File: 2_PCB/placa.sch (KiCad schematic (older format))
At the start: 39 parts, among them J1 Screw_Terminal_01x02, J2 Conn_01x04_Male, J3 Screw_Terminal_01x02, J4 TestPoints, J5 Conn_01x02_Male, U1 STM32L051C8Tx, U2 Ai-Thinker-Ra-01, Y1 8 MHz, Y2 32.768 kHz

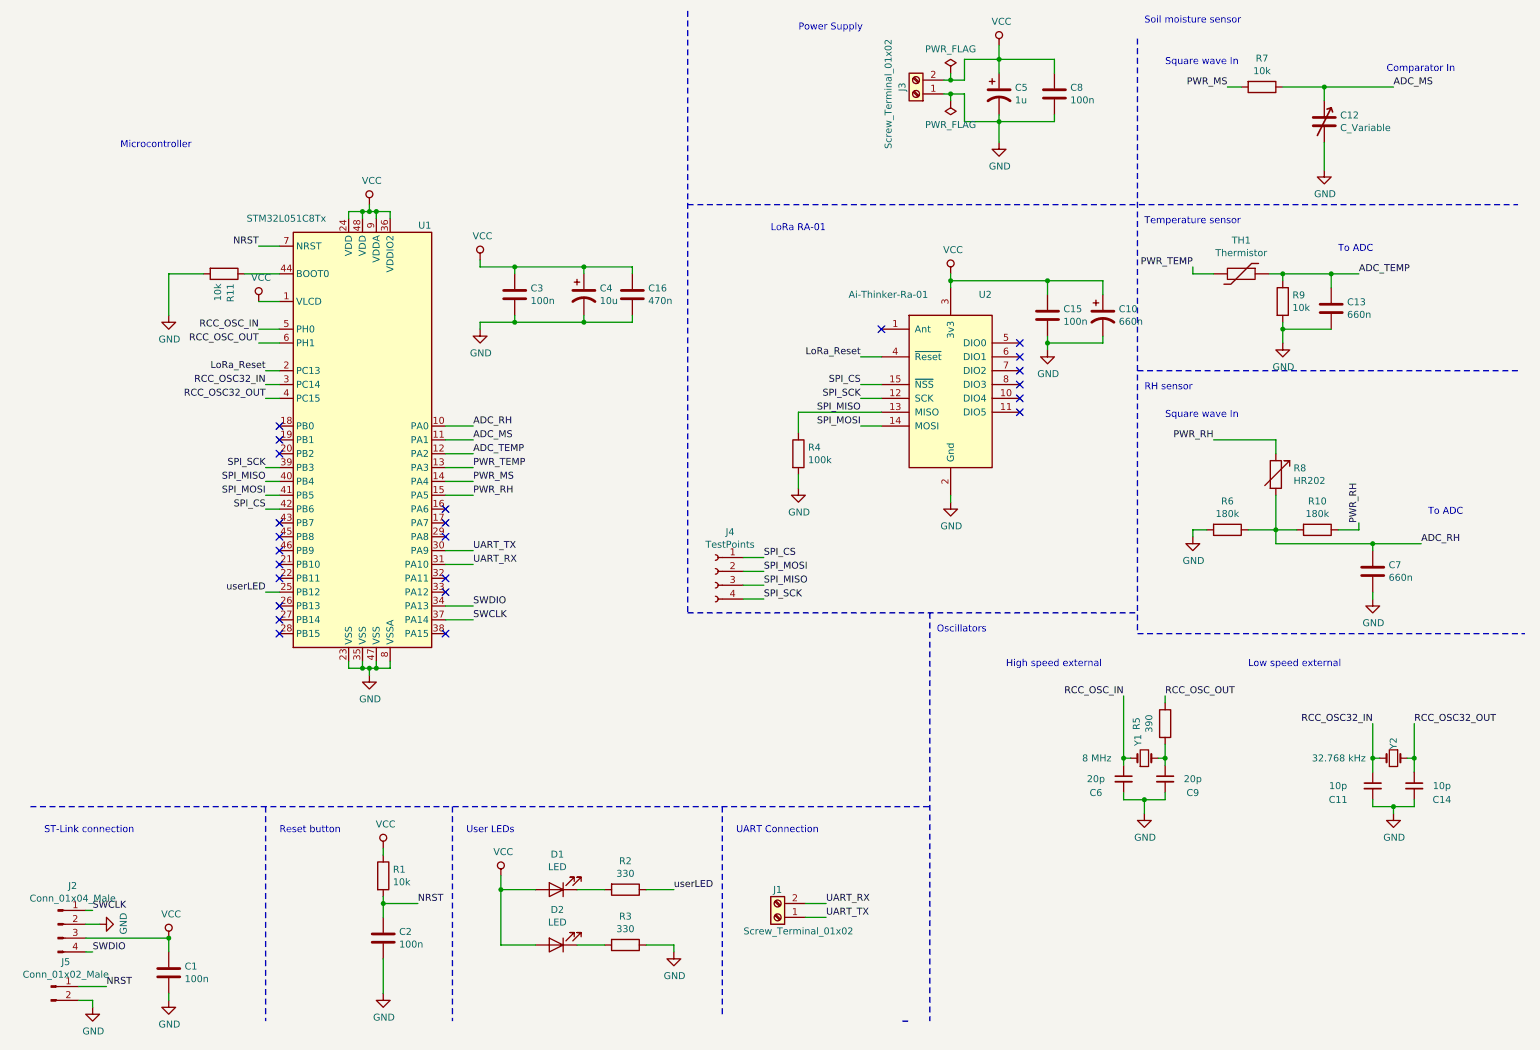
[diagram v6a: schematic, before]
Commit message: New branch for new HW revision. To add different layout, comparator for MS, change in RH circ
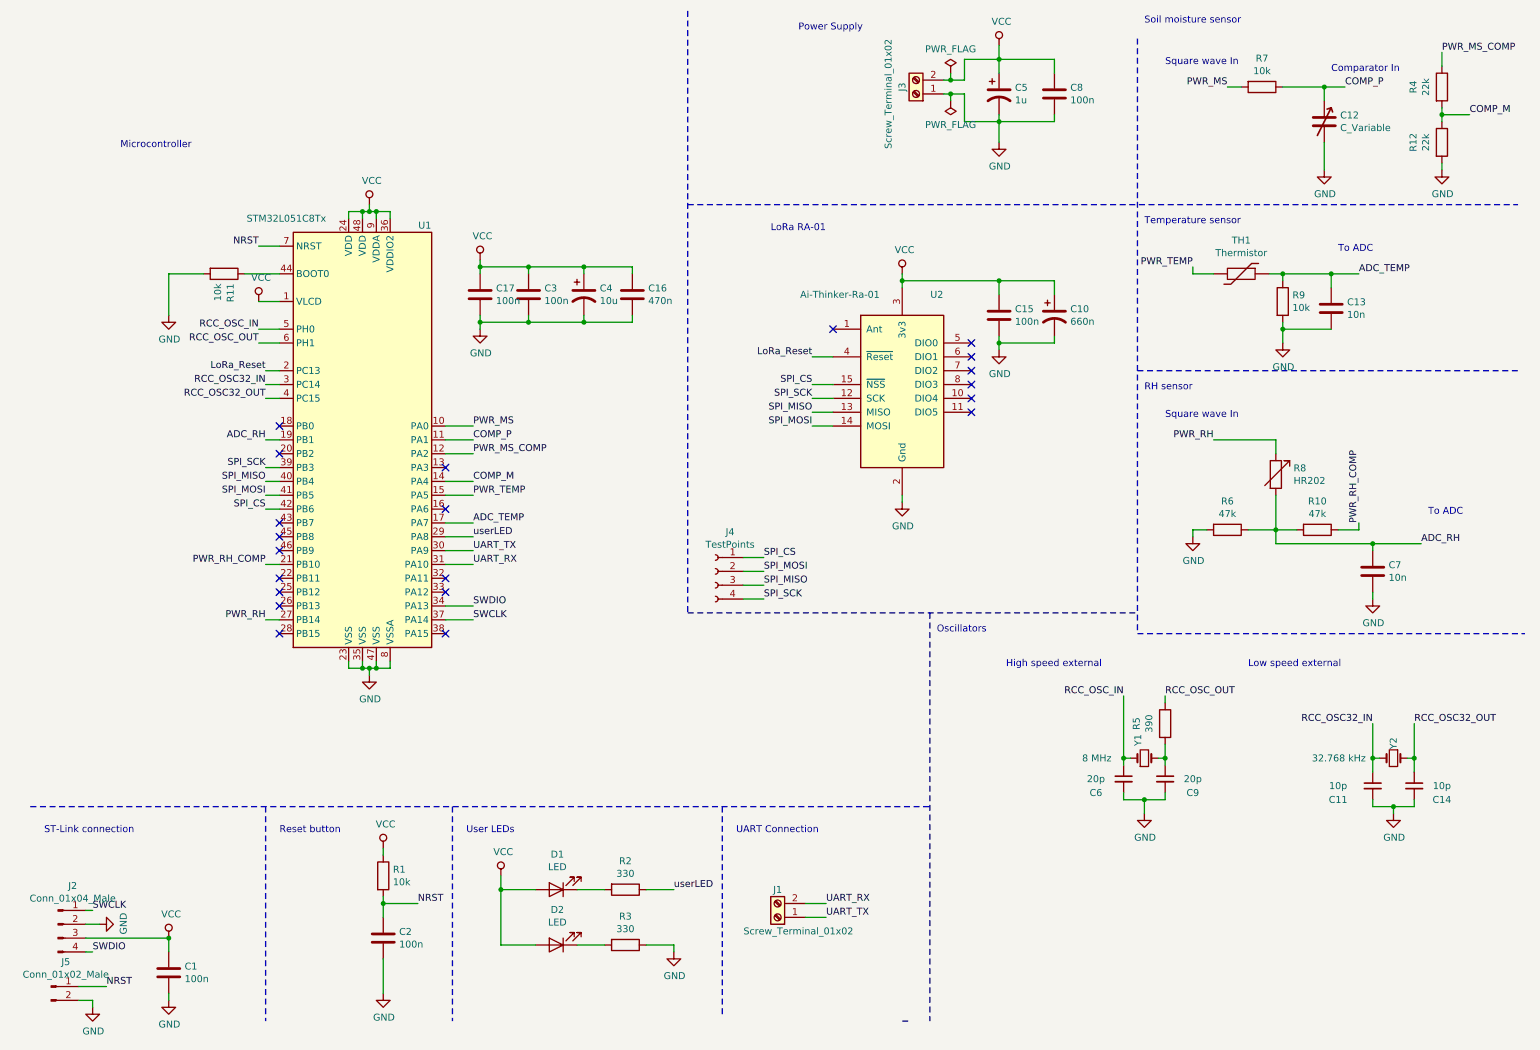
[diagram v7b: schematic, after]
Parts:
- added C17: 100n, Capacitor_SMD:C_0805_2012Metric_Pad1.15x1.40mm_HandSolder, symbol Device:C
- added R12: 22k, Resistor_SMD:R_0805_2012Metric_Pad1.15x1.40mm_HandSolder, symbol Device:R
- C13, C7: value 660n -> 10n
- R10, R6: value 180k -> 47k
- R4: value 100k -> 22k
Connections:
- net ADC_RH: now also U1.19 (PB1); no longer U1.10 (PA0)
- net ADC_TEMP: now also U1.17 (PA7); no longer U1.12 (PA2)
- net GND: now also C17.2, R12.2; no longer R4.2
- net PWR_MS: now also U1.10 (PA0); no longer U1.14 (PA4)
- net PWR_RH: now also U1.27 (PB14); no longer R10.1, U1.15 (PA5)
- net PWR_TEMP: now also U1.15 (PA5); no longer U1.13 (PA3)
- net SPI_MISO: no longer R4.1
- net VCC: now also C17.1
- net userLED: now also U1.29 (PA8); no longer U1.25 (PB12)
- net PWR_RH_COMP: now reaches U1.21 (PB10)
- net PWR_RH_COMP: now also R10.1
- net ADC_MS renamed COMP_P
- new net COMP_M: R12.1, R4.2, U1.14 (PA4)
- new net PWR_MS_COMP: R4.1, U1.12 (PA2)
- no-connect marks 24 -> 21
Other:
- moved on the sheet: C10, C15, C3, U2

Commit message: Adding new files
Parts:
- C7: value 10n -> 1n
- R7: value 10k -> 470k
- R8: footprint Resistor_THT:R_Box_L8.4mm_W2.5mm_P5.08mm -> Resistor_THT:R_Axial_DIN0204_L3.6mm_D1.6mm_P1.90mm_Vertical
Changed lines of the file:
@@
 P 9350 1050
 F 0 "R7" V 9143 1050 50  0000 C CNN
-F 1 "10k" V 9234 1050 50  0000 C CNN
+F 1 "470k" V 9234 1050 50  0000 C CNN
 F 2 "Resistor_SMD:R_0805_2012Metric_Pad1.15x1.40mm_HandSolder" V 9280 1050 50  0001 C CNN
 F 3 "~" H 9350 1050 50  0001 C CNN
@@
 F 0 "R8" H 9578 3896 50  0000 L CNN
 F 1 "HR202" H 9578 3805 50  0000 L CNN
-F 2 "Resistor_THT:R_Box_L8.4mm_W2.5mm_P5.08mm" V 9380 3850 50  0001 C CNN
+F 2 "Resistor_THT:R_Axial_DIN0204_L3.6mm_D1.6mm_P1.90mm_Vertical" V 9380 3850 50  0001 C CNN
 F 3 "~" H 9450 3850 50  0001 C CNN
 	1    9450 3850
@@
 P 10150 4550
 F 0 "C7" H 10265 4596 50  0000 L CNN
-F 1 "10n" H 10265 4505 50  0000 L CNN
+F 1 "1n" H 10265 4505 50  0000 L CNN
 F 2 "Capacitor_SMD:C_0805_2012Metric_Pad1.15x1.40mm_HandSolder" H 10188 4400 50  0001 C CNN
 F 3 "~" H 10150 4550 50  0001 C CNN
